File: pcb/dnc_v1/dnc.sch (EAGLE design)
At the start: 124 parts, among them IC1 LM2596S, IC2 74S244DW, Q1 IRF9321PBF, Q10 BSS316, Q11 BSS316, Q12 BSS138, Q2 BSS670, Q3 BSS138, Q4 BSS670, Q5 BSS138, Q6 BSS670, Q7 BSS138, Q8 BSS138, Q9 BSS670, U1 MAX202CDWR, U2 74HCT595D, U3 TC7SU04F, U4 AL8807, U5 AL8807

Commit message: clean board
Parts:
- removed C3, C4, C5, C6: 0.1uF, rcl:C-EUC0603
- removed R0, RBAT26: 100K, SparkFun-Passives:RESISTOR0603-RES
- removed RCODE: (no value), SparkFun-Passives:RESISTOR0603-RES
- removed RRST: 10K, rcl:R-EU_R0603
- added C19, C20, C28: 0.1uF, rcl:C-EUC0603
- added C21: 1uF, rcl:C-EUC0603
- added R26: 100K, SparkFun-Passives:RESISTOR0603-RES
- added R40: 10K, SparkFun-Passives:RESISTOR0603-RES
- added R41, R42: 220, SparkFun-Passives:RESISTOR0603-RES
- C1: value (none) -> 680uF30mm; device rcl:CPOL-USE -> SparkFun:CAP_POLPTH4
- C10, C11, C12: value 1uF -> 0.1uF
- C14, C15: value 0.1uF -> 1uF
- C2: value 680uF30mm -> (none); device SparkFun:CAP_POLPTH4 -> rcl:CPOL-USE
- R1: value 100k1% -> 100K
- R10, R11, R9: value 100K -> 33K
- R12: value 100K -> (none)
- R14, R15: value 0.110 -> 100K
- R2: value 10k1% -> 100k1%
- R21: value 100K -> 10K; device SparkFun-Passives:RESISTOR0603-RES -> rcl:R-EU_R0603
- R22: value 10K -> 100K
- R23: value 20K -> 0.110
- R24: value 10K -> 0.110
- R25: value 20K -> 100K
- R28, R30: value 220 -> 100K
- R3: value 100K -> 10k1%
- R31, R32: value 56K -> 100K
- R33: value 33K -> 20K
- R34, R36: value 33K -> 10K
- R35: value 56K -> 20K
- R37: value 1K -> 10K
- R5: value 100K -> 1K
- R6, R7: value 10K -> 56K
- R8: value 100K -> 56K
- renumbered C3.1 to C27, C3.2 to C25, C7 to C24, C8 to C23, C9 to C22, CRST to C26, LEDG to LG, LEDR to LR
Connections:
- net LEDG renamed LG
- net +3V3: now also R38.2; no longer R6.2
- net +5V: now also C11.1, C12.1, C19.1, C2.+, C28.1, R14.2, R15.2, R16.2, R17.2, R18.2, R19.2, R20.2, R21.2, R41.2, R42.2, R6.2; no longer C1.+, C14.1, C15.1, C18.1, C4.1, R10.2, R11.2, R12.2, R28.2, R30.2, R31.2, R32.2, R35.2, R4.2, R9.2, RRST.2
- net ANALOG_RAW: now also R3.2; no longer R2.2
- net CODE: now also R12.1; no longer RCODE.1
- net CS_TRIGGER_ACTIVE_HIGH: now also R39.2; no longer R38.2
- net GND: now also C10.2, C14.2, C20.2, C28.2, R1.2, R12.2, R22.1, R26.1, R28.1, R3.1, R30.1, R31.1, R32.1, R33.1, R35.1, R4.1, R40.1; no longer C17.2, C18.2, C3.2, C4.2, R0.1, R16.1, R17.1, R18.1, R19.1, R2.1, R20.1, R21.1, R23.1, R3.2, R38.1, RBAT26.1, RCODE.2
- net GYRO_1: now also R28.2; no longer R16.2
- net GYRO_2: now also R27.2; no longer R17.2
- net GYRO_3: now also R26.2; no longer R18.2
- net GYRO_4: now also R25.2; no longer R19.2
- net INT_ATMEGA: now also R35.2, R36.1; no longer R22.1, R23.2
- net INT_ATMEGA_5V: now also R36.2; no longer R22.2
- net INT_TELECO: now also R33.2, R34.1; no longer R24.1, R25.2
- net INT_TELECO_5V: now also R34.2; no longer R24.2
- net LED+1: now also R24.1; no longer R14.1
- net LED+2: now also C21.1, R23.1; no longer C10.1, R15.1
- net LED-2: now also C21.2; no longer C10.2
- net LED_G: now also R31.2; no longer R29.2
- net LED_R: now also R32.2; no longer R27.2
- net MISO: now also R38.1; no longer R6.1
- net MISO_5V: now also R37.1; no longer R7.1
- net N$18: now also R41.1; no longer R30.1
- net N$20: now also R10.1, R7.1; no longer R32.1, R34.1
- net N$21: now also R42.1; no longer R28.1
- net N$22: now also R6.1, R9.1; no longer R31.1, R33.1
- net N$23: now also R11.1, R8.1; no longer R35.1, R36.1
- net N$24: now also C19.2; no longer C14.2
- net N$25: now also R5.1; no longer R37.1
- net N$3: now also R2.1; no longer R1.1
- net N$35: now also C20.1; no longer C17.1
- net N$50: now also C18.2; no longer C6.2
- net N$51: now also C18.1; no longer C6.1
- net N$52: now also C17.2; no longer C5.2
- net N$53: now also C17.1; no longer C5.1
- net PROTECT_GATE: now also R1.1; no longer R3.1
- net PUSH1: now also C15.1, R9.2; no longer C13.1, R33.2
- net PUSH2: now also C14.1, R10.2; no longer C12.1, R34.2
- net PUSH3: now also C13.1, R11.2; no longer C11.1, R36.2
- net PWM_FLEX_1: now also R30.2; no longer R20.2
- net PWM_FLEX_2: now also R29.2; no longer R21.2
- net RAW_FUSED: now also C1.+, C10.1, R2.2, R23.2, R24.2; no longer C2.+, C3.1, R1.2, R14.2, R15.2
- net READ_BATTERY: now also R4.2; no longer R0.2
- net RELAY1: now also R22.2; no longer RBAT26.2
- net RESET: now also R21.1; no longer RRST.1
- net RST1: now also R16.1; no longer R9.1
- net RST2: now also R14.1; no longer R5.1
- net RST3: now also R13.1; no longer R4.1
- net RST4: now also R15.1; no longer R8.1
- net RST5: now also R19.1; no longer R12.1
- net RST6: now also R20.1; no longer R13.1
- net RST7: now also R17.1; no longer R10.1
- net RST8: now also R18.1; no longer R11.1
- net SCK_5V: now also R40.2; no longer R39.2
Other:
- moved on the sheet: C1, C10, C11, C12, C13, C14, C15, C17, C18, C2, R1, R10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

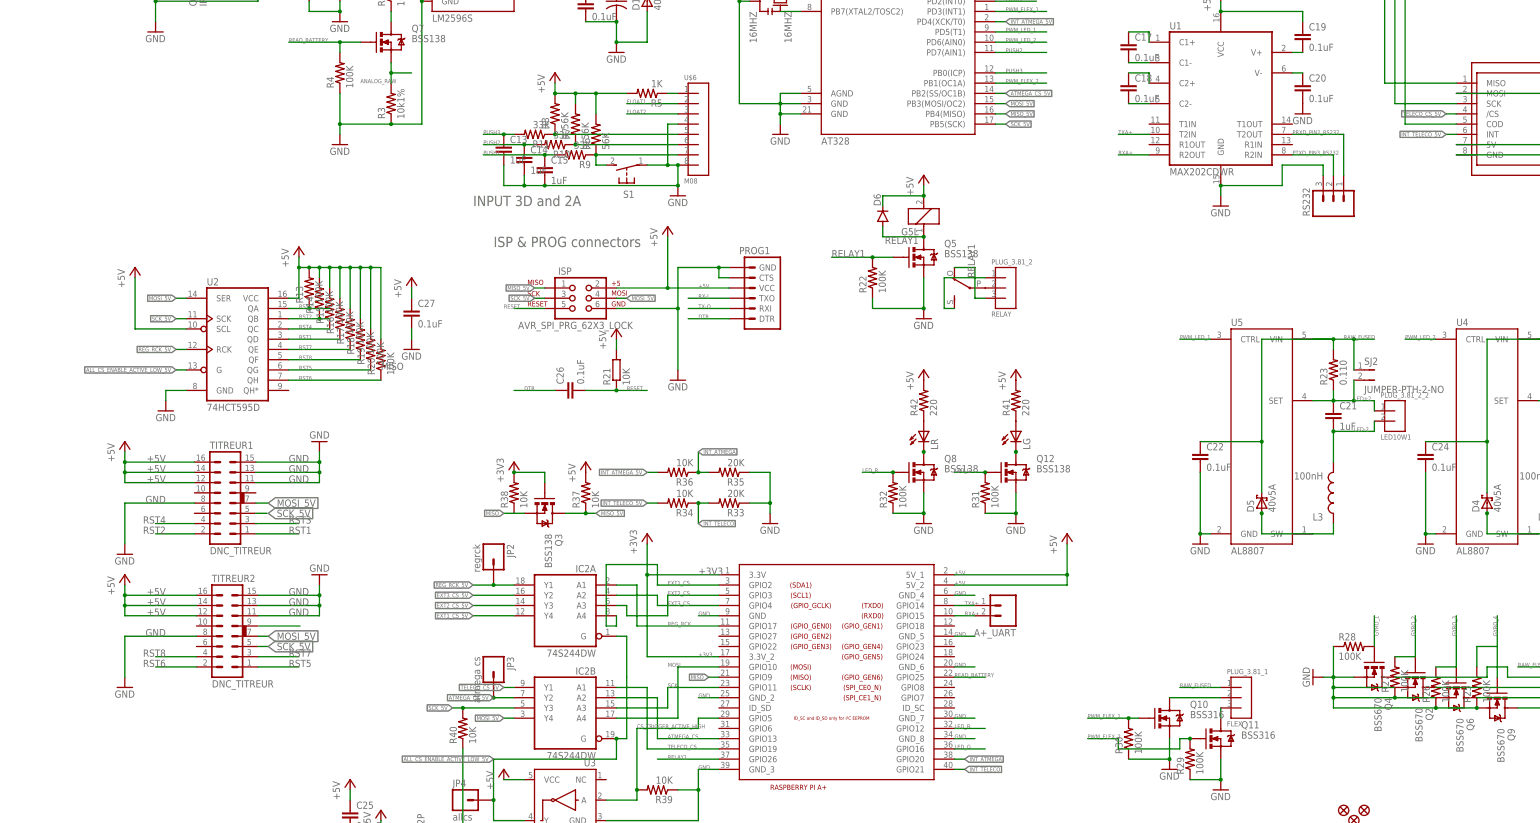
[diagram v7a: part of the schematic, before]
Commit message: rj45 au dessus
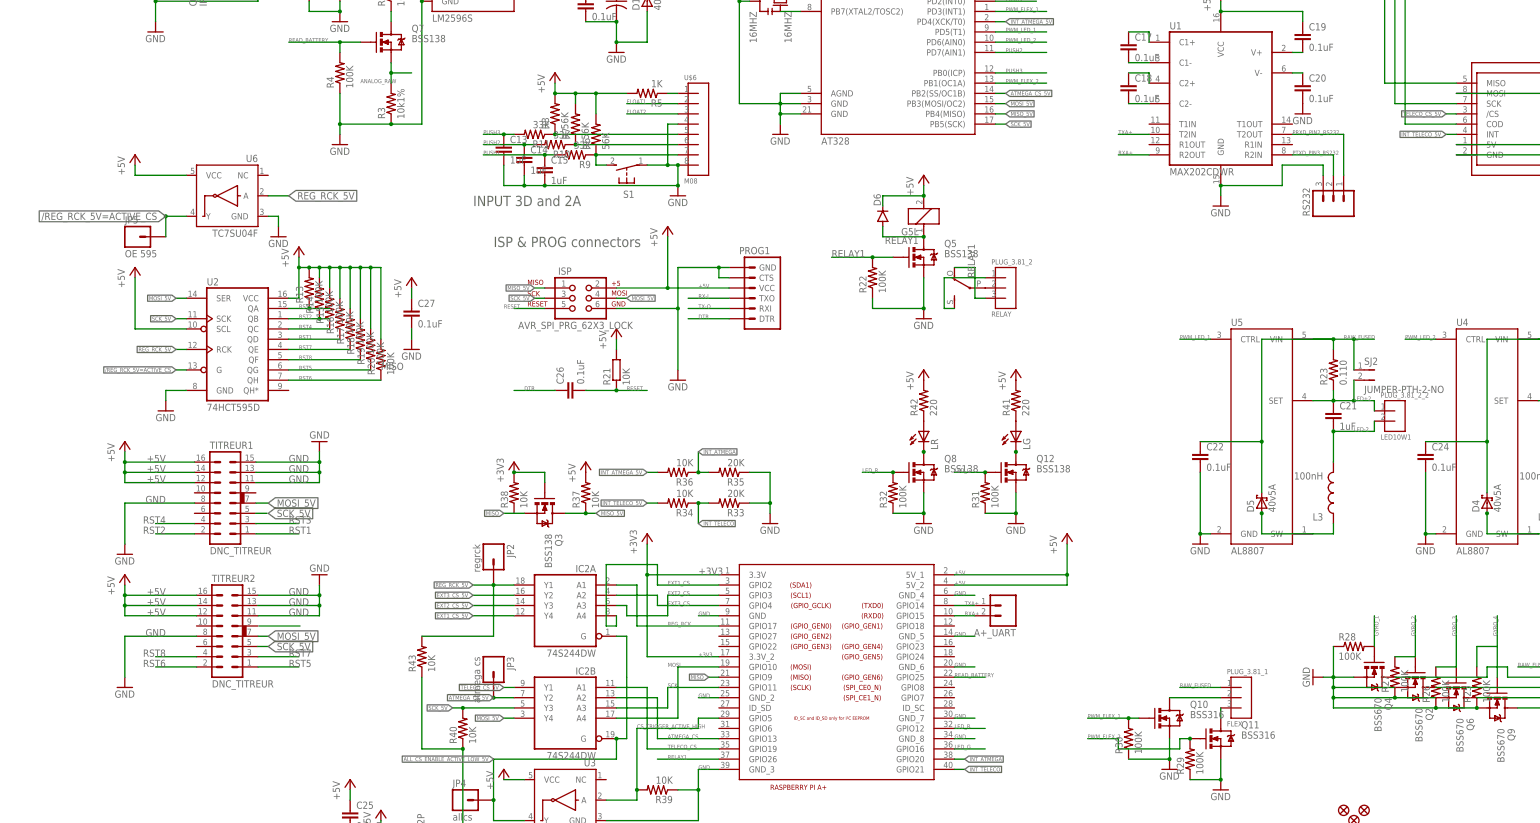
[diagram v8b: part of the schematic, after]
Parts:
- added JP5: OE 595, SparkFun-Connectors:M01PTH
- added R43: 10K, SparkFun-Passives:RESISTOR0603-RES
- added U6: TC7SU04F, SparkFun-DigitalIC:INVERTER_SOT23-5
- RS232: device SparkFun-Connectors:M03LOCK_LONGPADS -> SparkFun-Connectors:M03LOCK
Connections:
- new net /REG_RCK_5V=ACTIVE_CS: JP5.1, U2.G, U6.Y
- net +5V: now also U6.VCC
- net ALL_CS_ENABLE_ACTIVE_LOW_5V: no longer U2.G
- net GND: now also R43.1, U6.GND
- net REG_RCK_5V: now also R43.2, U6.A
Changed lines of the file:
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@@
 <part name="GND17" library="SparkFun" deviceset="GND" device=""/>
 <part name="P+22" library="supply1" deviceset="+5V" device=""/>
-<part name="RS232" library="SparkFun-Connectors" deviceset="M03" device="LOCK_LONGPADS"/>
+<part name="RS232" library="SparkFun-Connectors" deviceset="M03" device="LOCK"/>
+<part name="U6" library="SparkFun-DigitalIC" deviceset="INVERTER" device="_SOT23-5" value="TC7SU04F"/>
+<part name="P+23" library="supply1" deviceset="+5V" device=""/>
+<part name="GND18" library="SparkFun" deviceset="GND" device=""/>
+<part name="JP5" library="SparkFun-Connectors" deviceset="M01" device="PTH" value="OE 595"/>
+<part name="R43" library="SparkFun-Passives" deviceset="RESISTOR" device="0603-RES" value="10K"/>
 </parts>
 <sheets>
@@
 <instance part="P+22" gate="1" x="264.16" y="223.52" rot="R90"/>
 <instance part="RS232" gate="G$1" x="307.34" y="165.1" rot="R90"/>
+<instance part="U6" gate="G$1" x="33.02" y="167.64" rot="MR0"/>
+<instance part="P+23" gate="1" x="10.16" y="177.8"/>
+<instance part="GND18" gate="1" x="45.72" y="157.48"/>
+<instance part="JP5" gate="G$1" x="10.16" y="157.48"/>
+<instance part="R43" gate="G$1" x="81.28" y="53.34" rot="R90"/>
 </instances>
 <busses>
@@
 <segment>
 <pinref part="U$4" gate="G$1" pin="GND_3"/>
-<wire x1="154.94" y1="25.4" x2="149.86" y2="25.4" width="0.1524" layer="91"/>
 <label x="149.86" y="25.4" size="1.016" layer="95"/>
 <pinref part="U3" gate="G$1" pin="GND"/>
+<wire x1="154.94" y1="25.4" x2="149.86" y2="25.4" width="0.1524" layer="91"/>
 <wire x1="127" y1="12.7" x2="149.86" y2="12.7" width="0.1524" layer="91"/>
 <wire x1="149.86" y1="12.7" x2="149.86" y2="20.32" width="0.1524" layer="91"/>
@@
 <wire x1="91.44" y1="10.16" x2="91.44" y2="30.48" width="0.1524" layer="91"/>
 <junction x="91.44" y="10.16"/>
+<pinref part="R43" gate="G$1" pin="1"/>
+<wire x1="81.28" y1="48.26" x2="81.28" y2="30.48" width="0.1524" layer="91"/>
+<wire x1="81.28" y1="30.48" x2="91.44" y2="30.48" width="0.1524" layer="91"/>
+<junction x="91.44" y="30.48"/>
 </segment>
 <segment>
@@
 <pinref part="C28" gate="G$1" pin="2"/>
 <pinref part="GND17" gate="1" pin="GND"/>
+</segment>
+<segment>
+<pinref part="GND18" gate="1" pin="GND"/>
+<wire x1="45.72" y1="160.02" x2="45.72" y2="162.56" width="0.1524" layer="91"/>
+<pinref part="U6" gate="G$1" pin="GND"/>
+<wire x1="45.72" y1="162.56" x2="43.18" y2="162.56" width="0.1524" layer="91"/>
 </segment>
 </net>
@@
 <pinref part="P+22" gate="1" pin="+5V"/>
 </segment>
+<segment>
+<pinref part="U6" gate="G$1" pin="VCC"/>
+<pinref part="P+23" gate="1" pin="+5V"/>
+<wire x1="22.86" y1="172.72" x2="10.16" y2="172.72" width="0.1524" layer="91"/>
+<wire x1="10.16" y1="172.72" x2="10.16" y2="175.26" width="0.1524" layer="91"/>
+</segment>
 </net>
 <net name="+3V3" class="2">
@@
 <wire x1="99.06" y1="71.12" x2="93.98" y2="71.12" width="0.1524" layer="91"/>
 <junction x="99.06" y="71.12"/>
+<pinref part="R43" gate="G$1" pin="2"/>
+<wire x1="81.28" y1="58.42" x2="99.06" y2="58.42" width="0.1524" layer="91"/>
+<wire x1="99.06" y1="58.42" x2="99.06" y2="71.12" width="0.1524" layer="91"/>
 </segment>
 <segment>
@@
 <label x="20.32" y="129.54" size="1.016" layer="95" rot="MR0" xref="yes"/>
 <pinref part="U2" gate="A" pin="RCK"/>
+</segment>
+<segment>
+<pinref part="U6" gate="G$1" pin="A"/>
+<wire x1="43.18" y1="167.64" x2="48.26" y2="167.64" width="0.1524" layer="91"/>
+<label x="48.26" y="167.64" size="1.778" layer="95" xref="yes"/>
 </segment>
 </net>
@@
 <junction x="99.06" y="17.78"/>
 </segment>
-<segment>
-<pinref part="U2" gate="A" pin="G"/>
-<wire x1="20.32" y1="124.46" x2="22.86" y2="124.46" width="0.1524" layer="91"/>
-<label x="20.32" y="124.46" size="1.016" layer="95" rot="MR0" xref="yes"/>
-</segment>
 </net>
 <net name="LG" class="0">
@@
 </segment>
 </net>
+<net name="/REG_RCK_5V=ACTIVE_CS" class="0">
+<segment>
+<pinref part="U6" gate="G$1" pin="Y"/>
+<wire x1="22.86" y1="162.56" x2="17.78" y2="162.56" width="0.1524" layer="91"/>
+<label x="17.78" y="162.56" size="1.778" layer="95" rot="MR0" xref="yes"/>
+<pinref part="JP5" gate="G$1" pin="1"/>
+<wire x1="17.78" y1="157.48" x2="17.78" y2="162.56" width="0.1524" layer="91"/>
+<junction x="17.78" y="162.56"/>
+</segment>
+<segment>
+<pinref part="U2" gate="A" pin="G"/>
+<wire x1="20.32" y1="124.46" x2="22.86" y2="124.46" width="0.1524" layer="91"/>
+<label x="20.32" y="124.46" size="1.016" layer="95" rot="MR0" xref="yes"/>
+</segment>
+</net>
